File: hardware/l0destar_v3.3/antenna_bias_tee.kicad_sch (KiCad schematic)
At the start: 13 parts

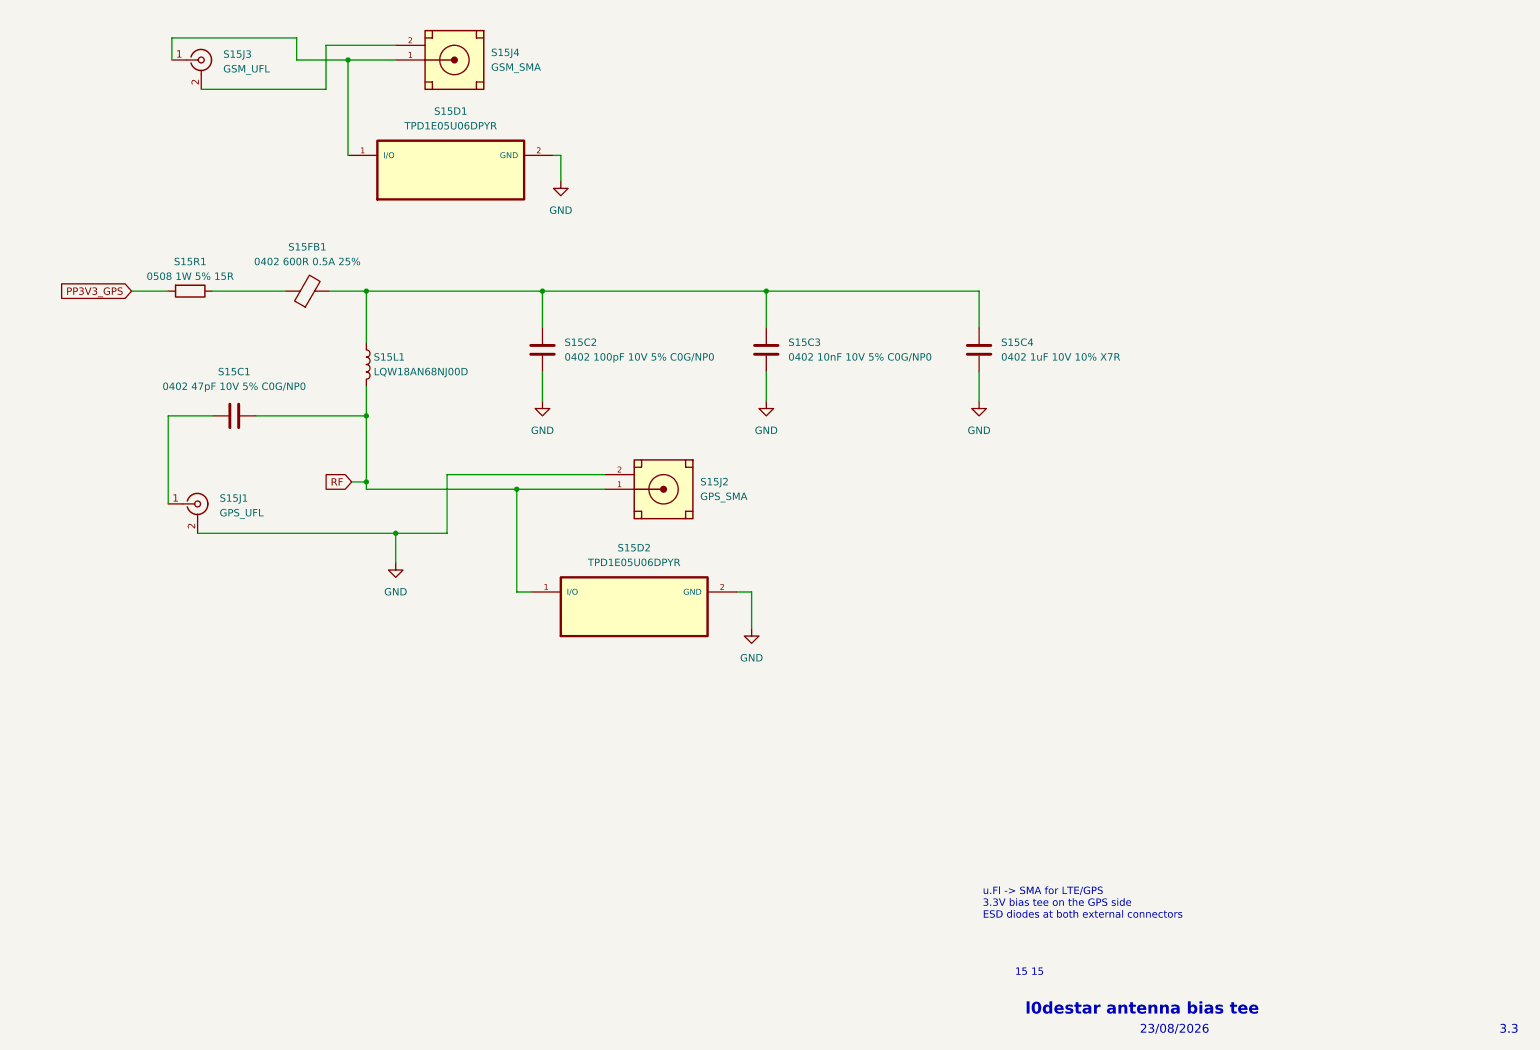
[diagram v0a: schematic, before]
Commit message: schematic<>readme discrepency fixes
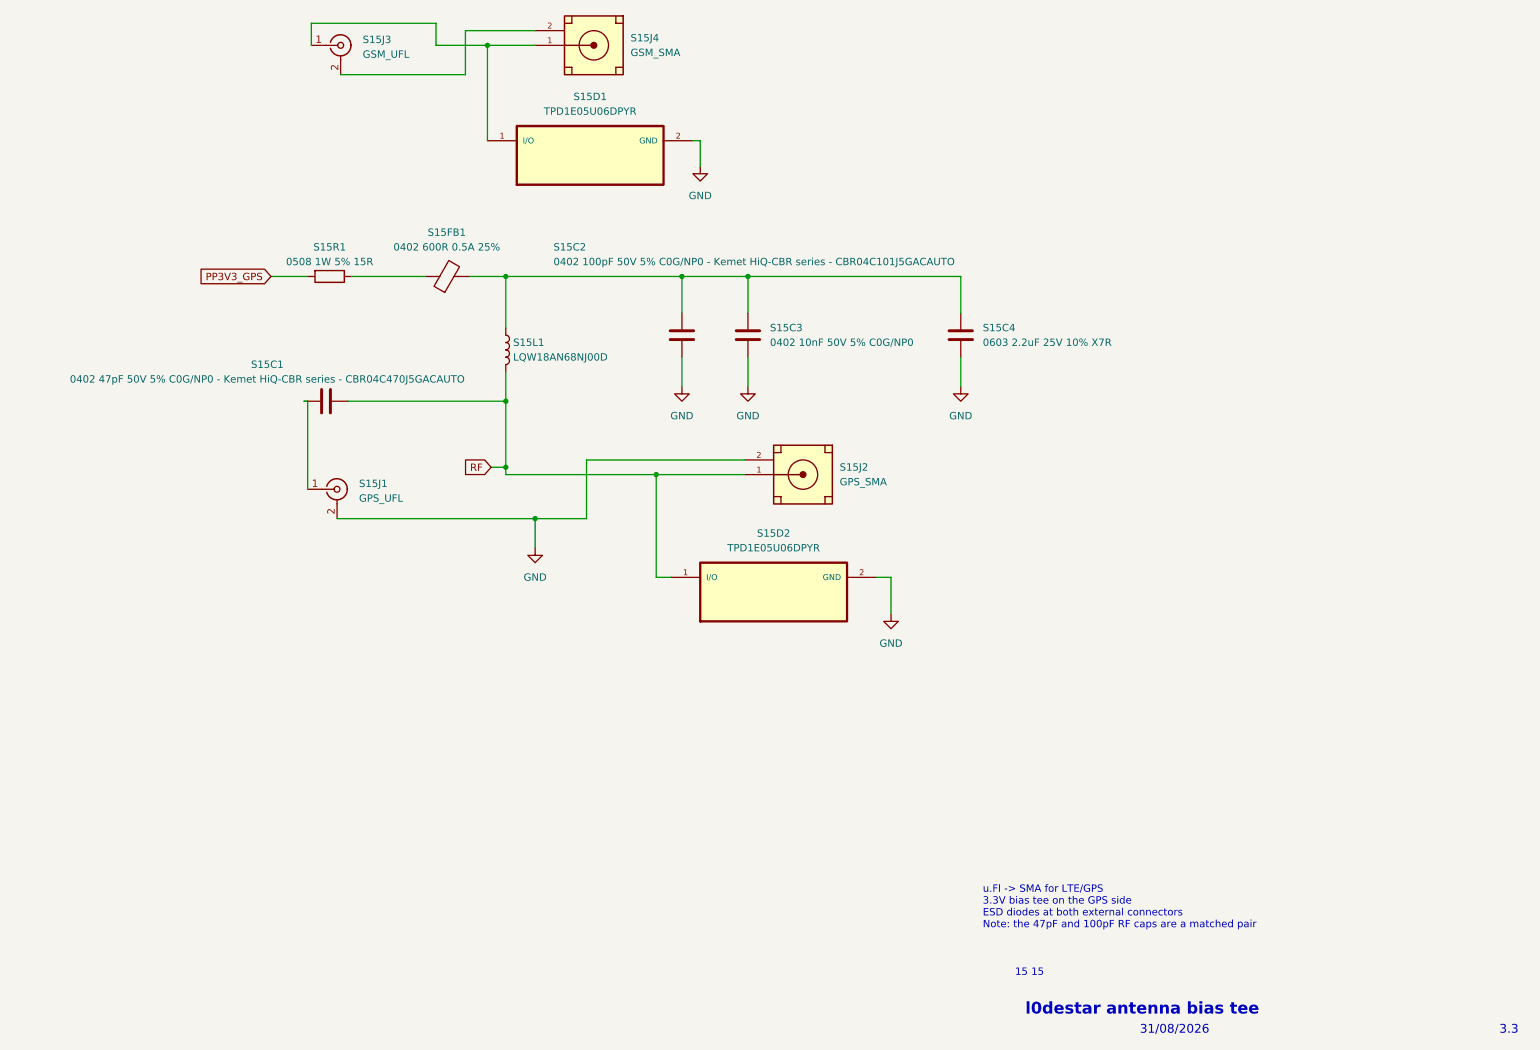
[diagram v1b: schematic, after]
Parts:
- S15C1: value 0402 47pF 10V 5% C0G/NP0 -> 0402 47pF 50V 5% C0G/NP0 - Kemet HiQ-CBR series - CBR04C470J5GACAUTO; Manufacturer_Name Multicomp Pro -> Kemet; Manufacturer_Part_Number 0402N470F500CT -> CBR04C470J5GACAUTO
- S15C2: value 0402 100pF 10V 5% C0G/NP0 -> 0402 100pF 50V 5% C0G/NP0 - Kemet HiQ-CBR series - CBR04C101J5GACAUTO; Manufacturer_Name Yageo -> Kemet; Manufacturer_Part_Number AC0402FRNPO9BN101 -> CBR04C101J5GACAUTO
- S15C3: value 0402 10nF 10V 5% C0G/NP0 -> 0402 10nF 50V 5% C0G/NP0
- S15C4: value 0402 1uF 10V 10% X7R -> 0603 2.2uF 25V 10% X7R; footprint Capacitor_SMD:C_0402_1005Metric -> Resistor_SMD:R_0603_1608Metric
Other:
- note added: "31/08/2026"
- note added: "u.Fl -> SMA for LTE/GPS 3.3V bias tee on the GPS side ESD diodes at both external connectors Note: the 47pF and 100pF RF caps are a matched pair"
- note removed: "23/08/2026"
- note removed: "u.Fl -> SMA for LTE/GPS 3.3V bias tee on the GPS side ESD diodes at both external connectors"
- moved on the sheet: S15C1, S15C2, S15C3, S15C4, S15D1, S15D2, S15FB1, S15J1, S15J2, S15J3, S15J4, S15L1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

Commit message: revised 3.3 board, parts and readme updates
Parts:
- S15C4: footprint Resistor_SMD:R_0603_1608Metric -> Capacitor_SMD:C_0603_1608Metric
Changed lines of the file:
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@@
 			)
 		)
-		(property "Footprint" "Resistor_SMD:R_0603_1608Metric"
+		(property "Footprint" "Capacitor_SMD:C_0603_1608Metric"
 			(at 176.2252 76.835 0)
 			(hide yes)

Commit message: fixed the 0508 footprint in v3.3 to actually match the part dimensions properly, saving precious microns of board real estate
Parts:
- S15R1: footprint Resistor_SMD:R_0508_1220Metric -> libs:R_0508_1220Metric_WideTerminal
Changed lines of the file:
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@@
 			)
 		)
-		(property "Footprint" "Resistor_SMD:R_0508_1220Metric"
+		(property "Footprint" "libs:R_0508_1220Metric_WideTerminal"
 			(at 66.04 61.087 90)
 			(hide yes)

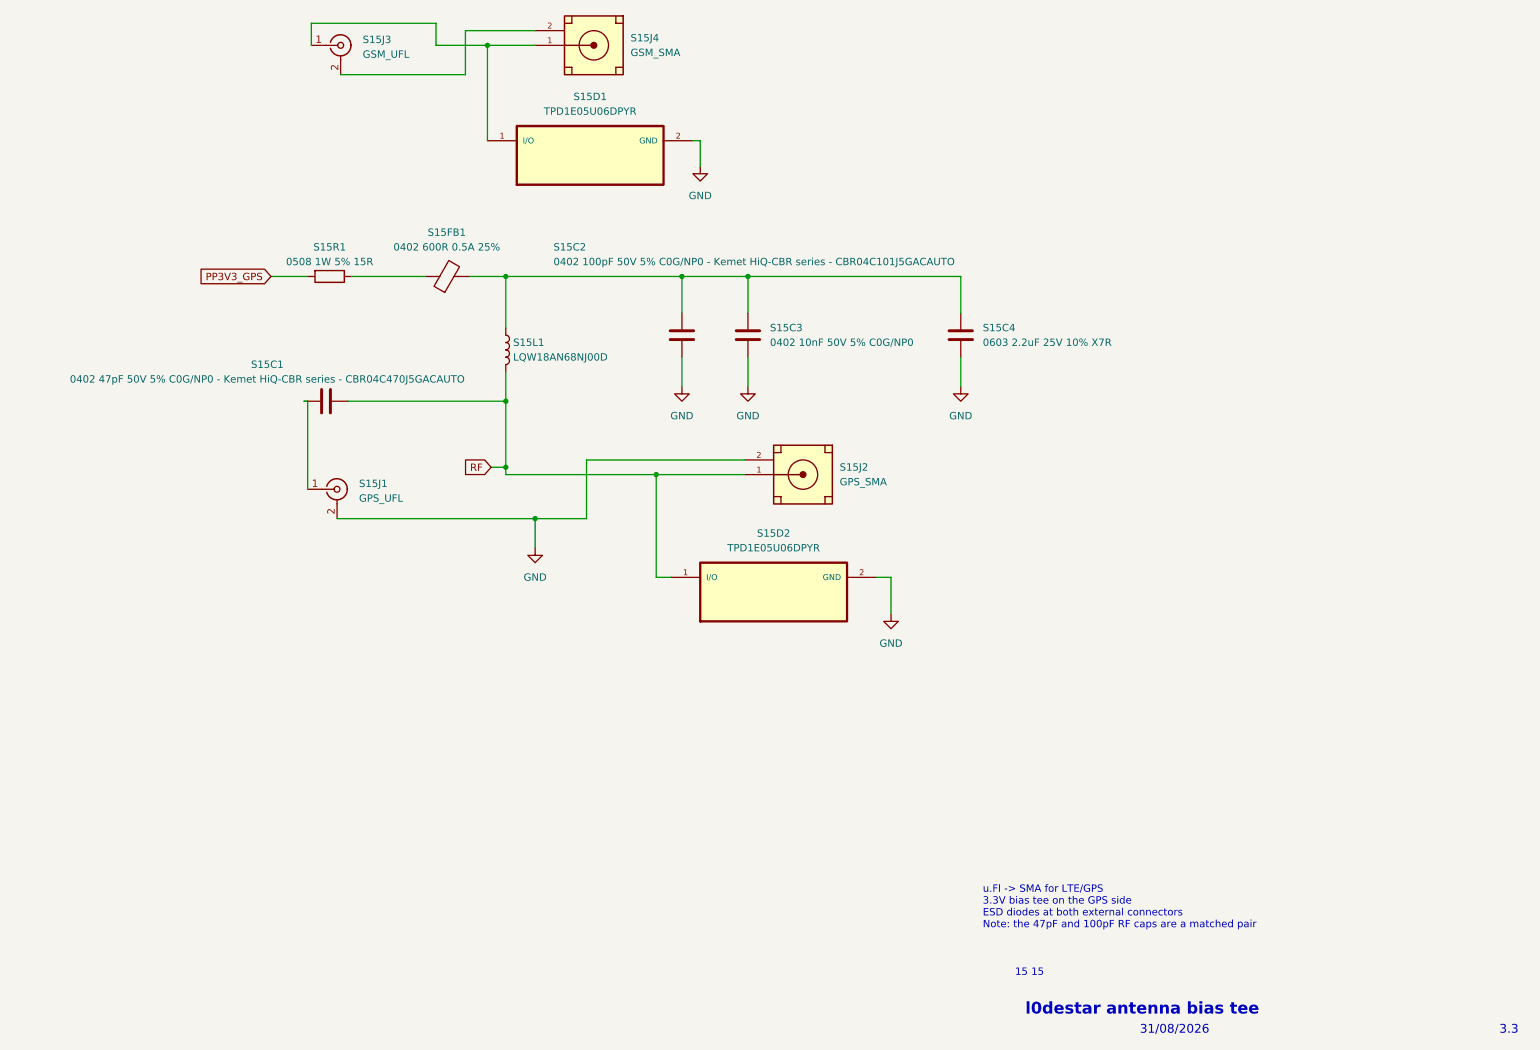
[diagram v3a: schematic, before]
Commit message: v3.3 RF optimisation
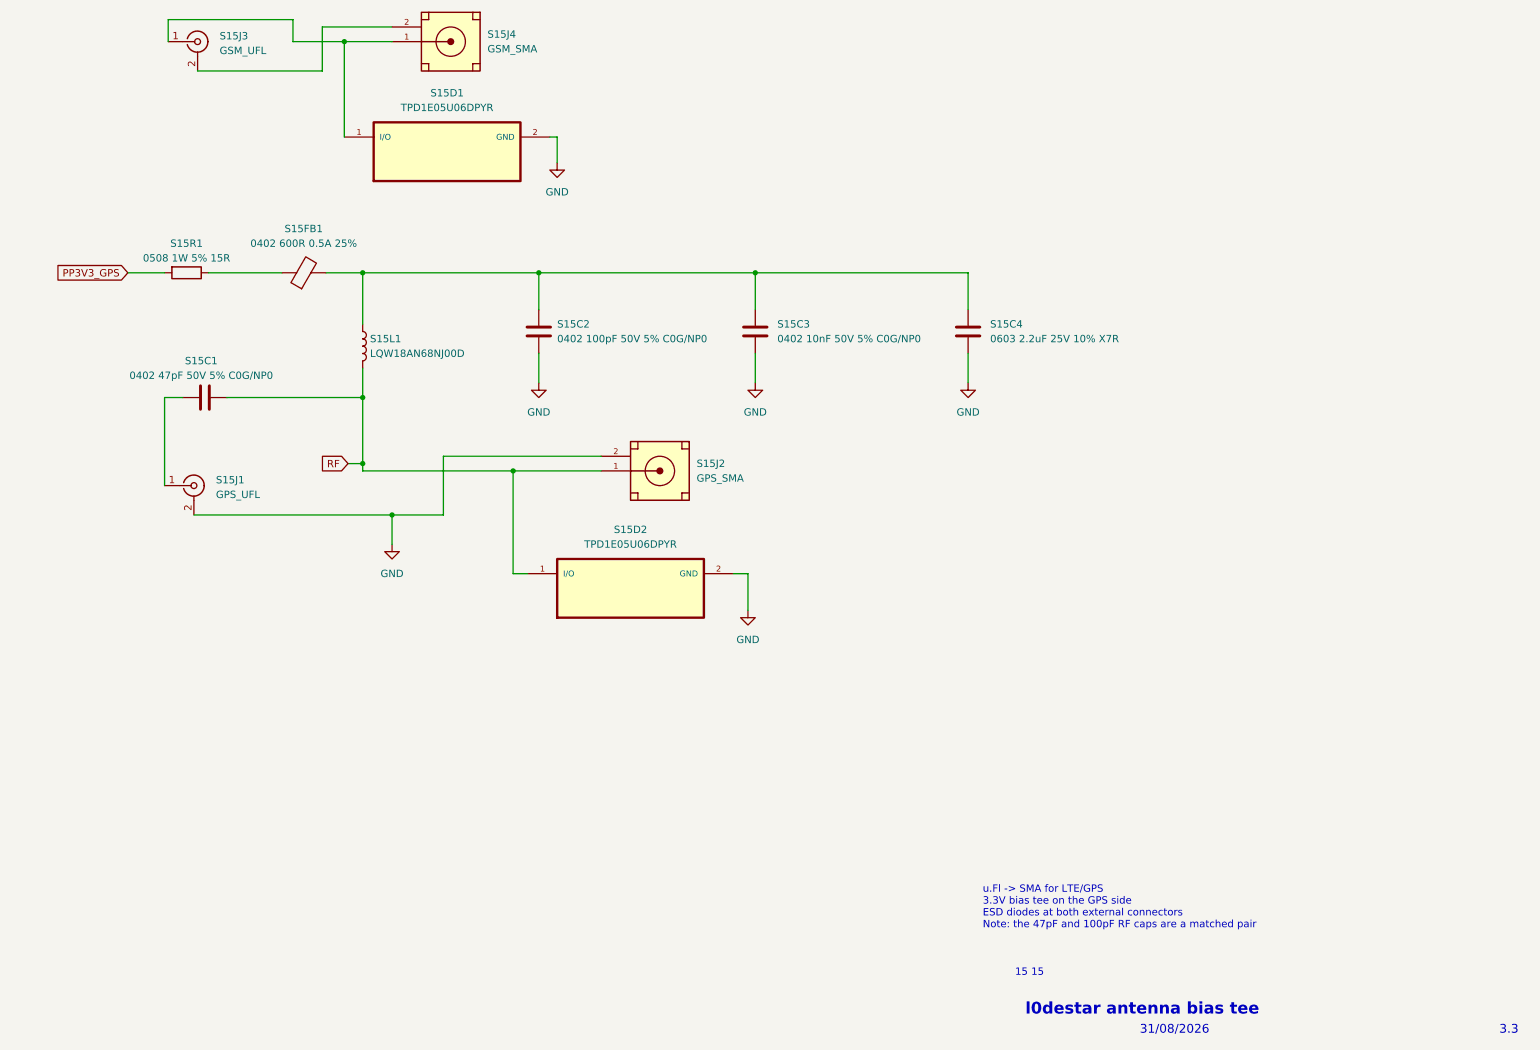
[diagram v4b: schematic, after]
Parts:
- S15C1: value 0402 47pF 50V 5% C0G/NP0 - Kemet HiQ-CBR series - CBR04C470J5GACAUTO -> 0402 47pF 50V 5% C0G/NP0; Manufacturer_Name Kemet -> (none); Manufacturer_Part_Number CBR04C470J5GACAUTO -> (none)
- S15C2: value 0402 100pF 50V 5% C0G/NP0 - Kemet HiQ-CBR series - CBR04C101J5GACAUTO -> 0402 100pF 50V 5% C0G/NP0; Manufacturer_Name Kemet -> (none); Manufacturer_Part_Number CBR04C101J5GACAUTO -> (none)
- S15J2, S15J4: footprint libs:SAMTEC_SMA-J-P-H-RA-TH1 -> libs:SAMTEC_SMA-J-P-H-RA-TH1_centrepin
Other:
- moved on the sheet: S15C1, S15C2, S15C3, S15C4, S15D1, S15D2, S15FB1, S15J1, S15J2, S15J3, S15J4, S15L1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
